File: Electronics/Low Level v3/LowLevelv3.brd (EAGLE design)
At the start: 117.3 x 68.1 mm, 58 parts, among them IC2 MCP4802, K1 ORWH-SH-105D1F,000, K3 ORWH-SH-105D1F,000, Q1 16MHz, T1 2N3904, T2 2N3904, U1 284512-4, U4 MCP2515, U5 MCP2551DIL08, X3 Motor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

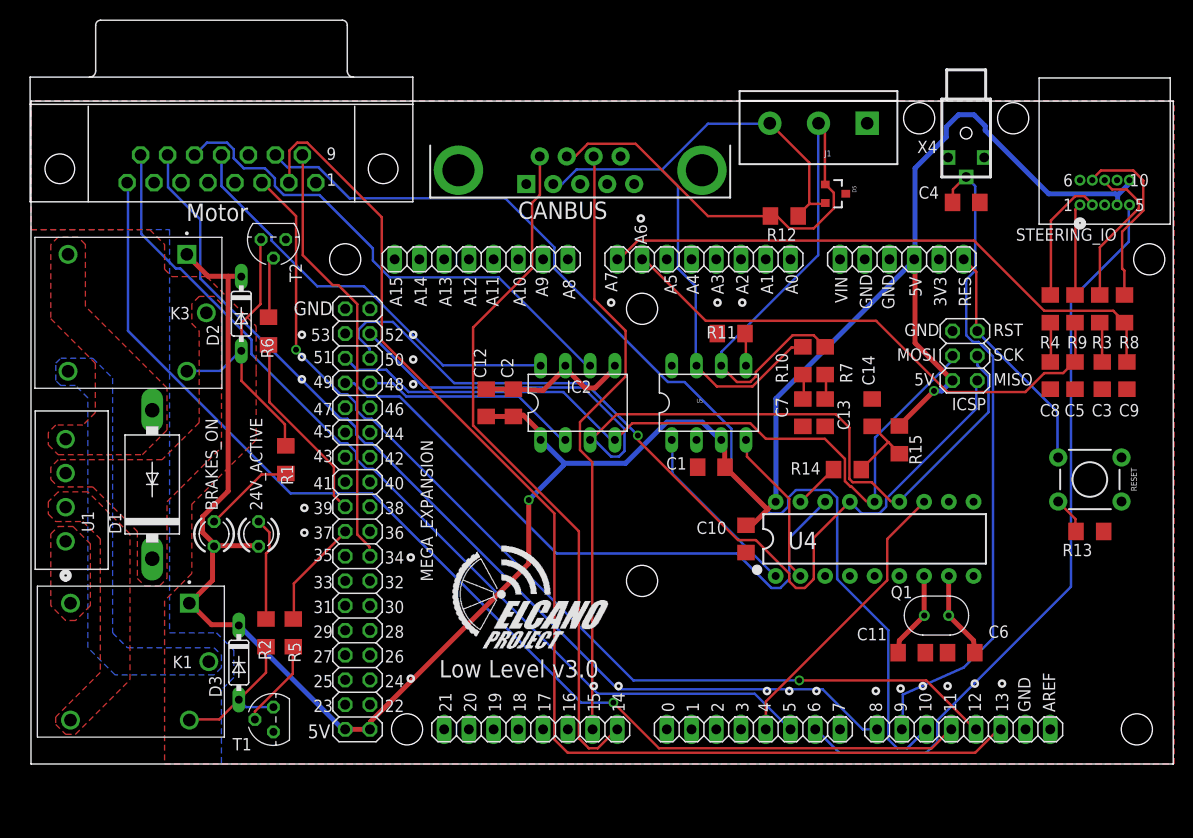
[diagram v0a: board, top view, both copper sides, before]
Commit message: Added e-stop, routed additional connetions to DB15, changed board layout
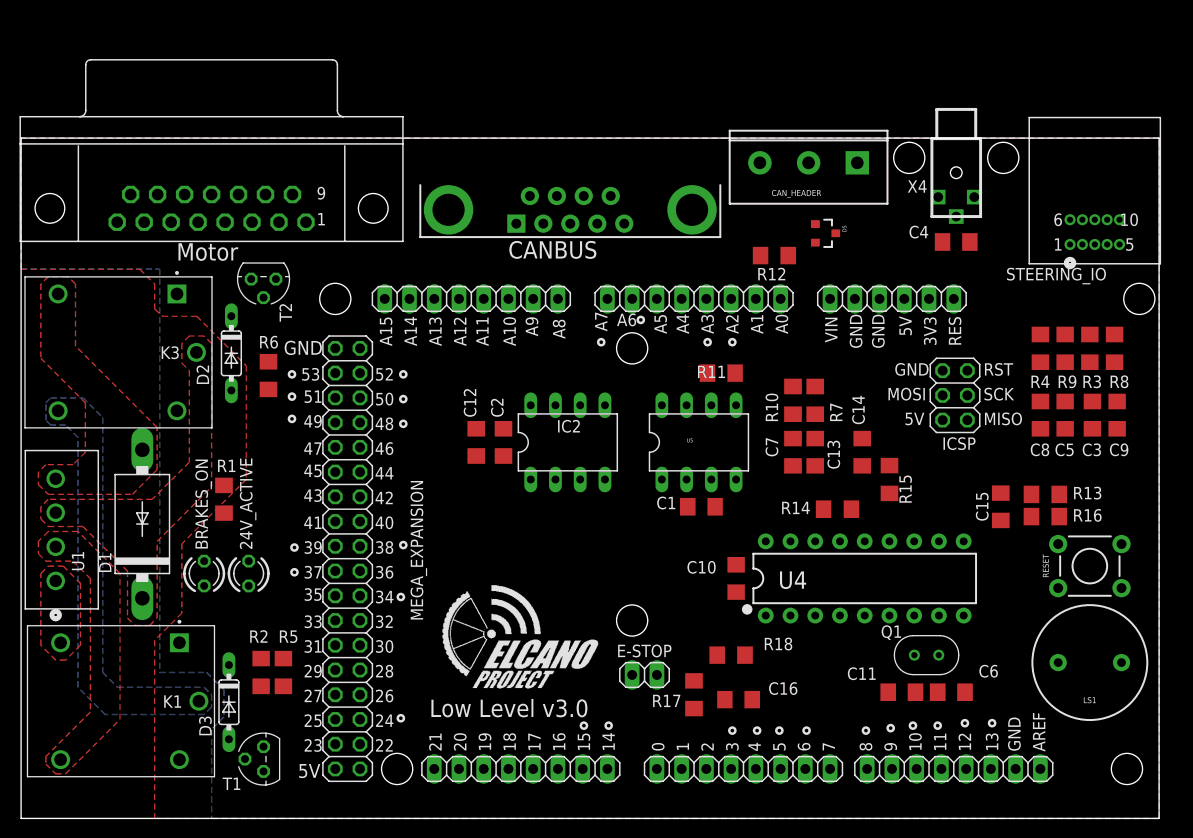
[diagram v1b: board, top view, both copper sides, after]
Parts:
- removed J1: (no value), SparkFun-Connectors:SCREWTERMINAL-5MM-3
- added C15, C16: 200nF, resistor:C1206
- added CAN_HEADER: (no value), SparkFun-Connectors:SCREWTERMINAL-5MM-3
- added E-STOP: (no value), pinhead:1X02
- added LS1: BUZZER-PTH, SparkFun-Electromechanical:BUZZER-12MM
- added R16, R17, R18: 10k, resistor:R1206
- R13: value 1K -> 10k
- moved RESET 8.89 mm to (109.7, 25.9), turned to 180 degrees
- moved R1 7.54 mm to (20.8, 32.8)
- moved R13 5.95 mm to (105.2, 33.3), turned to 0 degrees
- moved R6 4.57 mm to (25.4, 45.5)
- moved D5 4.19 mm to (82.5, 60.1)
- moved X4 4.19 mm to (96.0, 66.3)
- moved X3 4.19 mm to (19.6, 72.1)
- moved ADCL 4.19 mm to (69.1, 53.3)
- moved C1 4.19 mm to (69.8, 32.0)
- moved C12 4.19 mm to (46.7, 38.6)
- moved C14 4.19 mm to (86.4, 37.6)
- moved C3 4.19 mm to (110.0, 41.4)
- moved C4 4.19 mm to (96.0, 59.2)
- moved C8 4.19 mm to (104.6, 41.4)
- moved CANBUS 4.19 mm to (56.4, 62.5)
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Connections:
- net N$17 renamed OSC1
- net N$18 renamed OSC2
- removed net STR_L: ADCL.6
- removed net STR_R: ADCL.5
- new net BRAKE_PWM: DIGITAL_0-7.3, X3.1
- new net BUZZER: LS1.+, MEGA_EXPANSION.18
- new net D_36: MEGA_EXPANSION.20, X3.7
- new net ESTOP_INT: C16.1, DIGITAL_0-7.4, R17.1, X3.6
- new net N$8: E-STOP.2, R17.2, R18.1
- new net REGEN_ACTIVE: MEGA_EXPANSION.34, X3.5
- new net RX0: DIGITAL_0-7.1
- new net TX0: DIGITAL_0-7.2
- net 5V: now also E-STOP.1, RESET.1
- net CANH: now also CAN_HEADER.2; no longer J1.2
- net CANL: now also CAN_HEADER.3; no longer J1.3
- net GND: now also C15.2, C16.2, CAN_HEADER.1, LS1.-, R16.2, R18.2, U4.4, U4.5, U4.6; no longer J1.1, R13.1
- net L_SENSE: now also ADCL.6
- net N$1: now also R16.1
- net RESET: now also C15.1, R13.1; no longer RESET.1
- net REVERSE: now also X3.4
- net R_SENSE: now also ADCL.5
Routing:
- net 5V: track 241.2 -> 0.00 mm, vias 2 -> 0
- net HALLPHASEA: track 124.6 -> 0.00 mm
- net HALLPHASEC: track 118.4 -> 0.00 mm, vias 1 -> 0
- net EBIKECONTRL: track 110.9 -> 0.00 mm
- net HALLPHASEB: track 105.0 -> 0.00 mm, vias 2 -> 0
- net SPEEDOMETER: track 103.1 -> 0.00 mm
- net WATCHDOG: track 97.1 -> 0.00 mm
- net SCK: track 95.8 -> 0.00 mm
- net MISO: track 93.8 -> 0.00 mm, vias 1 -> 0
- net CANH: track 85.0 -> 0.00 mm
- net MOSI: track 81.5 -> 0.00 mm
- net STEER_SERVO_PWM: track 77.3 -> 0.00 mm
- net CANL: track 73.4 -> 0.00 mm
- net TX3: track 72.3 -> 0.00 mm
- net WHEELROTATION: track 67.6 -> 0.00 mm
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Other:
- board size 117.3 x 68.1 mm -> 116.8 x 69.8 mm

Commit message: partial routing, adding restrict polys
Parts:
- moved R11 3.34 mm to (75.2, 46.2), turned to 90 degrees
- moved R12 1.85 mm to (75.6, 58.3), turned to 90 degrees
- moved E-STOP 1.48 mm to (65.3, 15.5)
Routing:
- net 5V: track 0.00 -> 209.4 mm
- net HALLPHASEC: track 0.00 -> 138.1 mm, vias 0 -> 1
- net GND: track 0.00 -> 130.0 mm, vias 0 -> 4
- net WATCHDOG: track 0.00 -> 119.4 mm, vias 0 -> 1
- net SPEEDOMETER: track 0.00 -> 116.5 mm, vias 0 -> 1
- net HALLPHASEA: track 0.00 -> 114.9 mm, vias 0 -> 1
- net HALLPHASEB: track 0.00 -> 113.7 mm, vias 0 -> 1
- net EBIKECONTRL: track 0.00 -> 111.3 mm, vias 0 -> 1
- net REGEN_ACTIVE: track 0.00 -> 106.4 mm
- net SCK: track 0.00 -> 101.3 mm, vias 0 -> 2
- net ESTOP_INT: track 0.00 -> 101.1 mm, vias 0 -> 2
- net MISO: track 0.00 -> 91.0 mm, vias 0 -> 2
- net MOSI: track 0.00 -> 84.9 mm, vias 0 -> 2
- net BRAKE_PWM: track 0.00 -> 78.8 mm
- net CANH: track 0.00 -> 71.9 mm, vias 0 -> 1
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
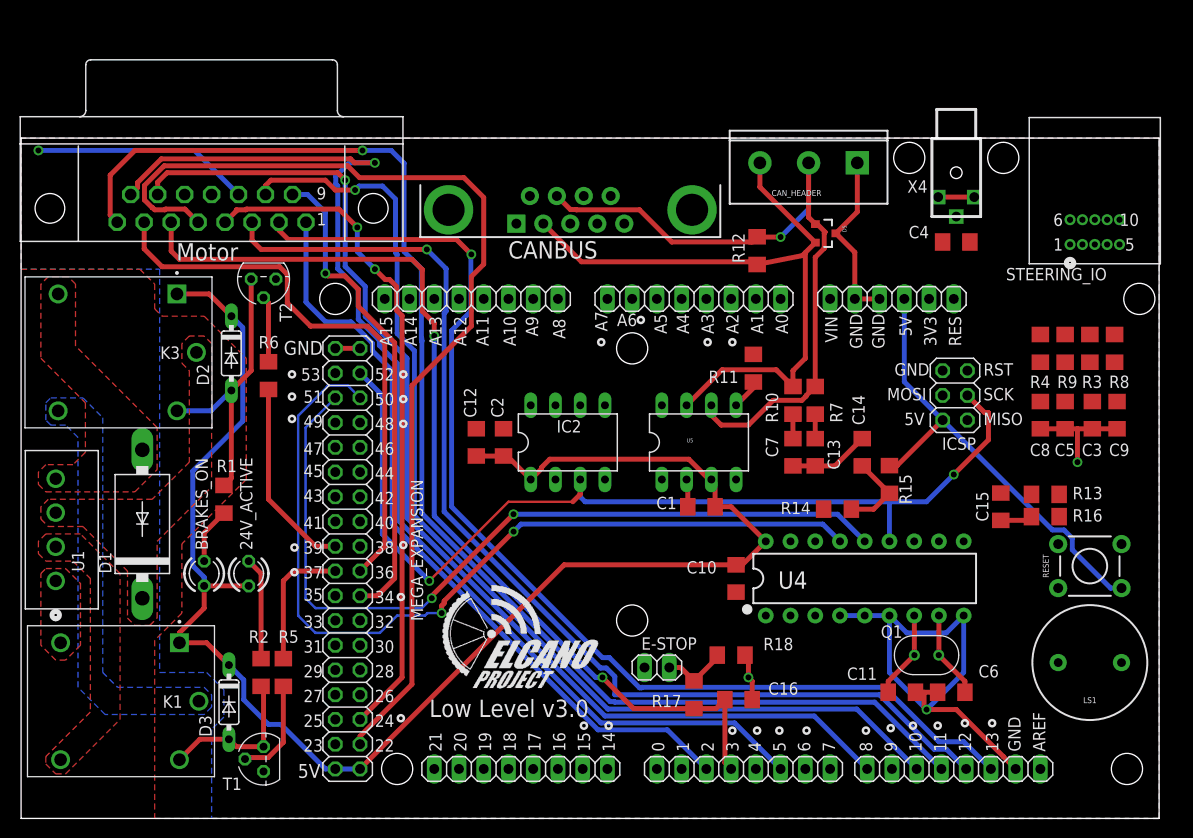
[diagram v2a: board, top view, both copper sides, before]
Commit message: LLBv3 routing overhaul
applied restriction polygons and added many vias to prevent GND airwires
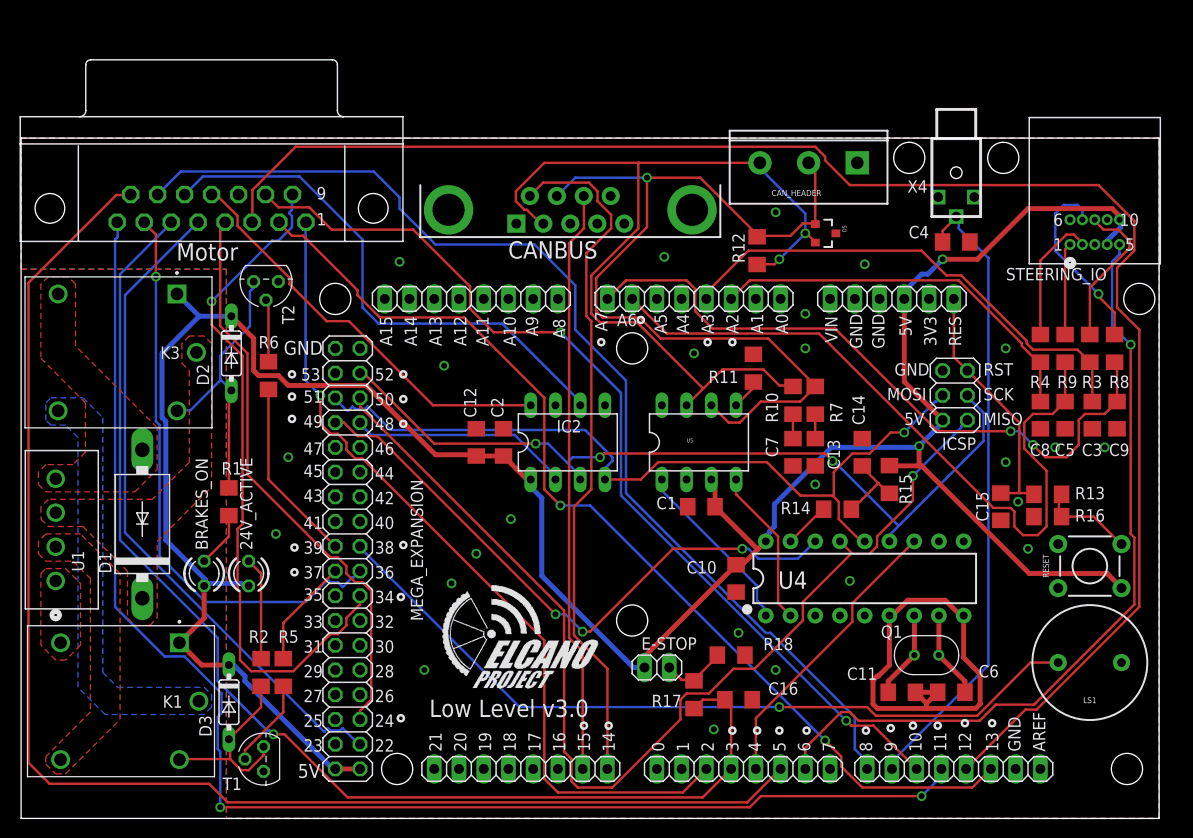
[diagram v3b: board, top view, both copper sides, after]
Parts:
- moved R1 0.57 mm to (21.3, 32.5)
- moved T2 0.36 mm to (25.1, 55.1)
- moved R13 0.25 mm to (105.4, 33.3)
- moved R16 0.25 mm to (105.4, 31.0)
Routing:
- net GND: track 130.0 -> 46.0 mm, vias 4 -> 25
- net BUZZER: track 0.00 -> 81.2 mm, vias 0 -> 1
- net STEER_SERVO_PWM: track 0.00 -> 81.0 mm, vias 0 -> 1
- net L_RTN_GND: track 0.00 -> 74.6 mm
- net TX3: track 0.00 -> 71.2 mm
- net R_RTN_GND: track 0.00 -> 70.0 mm, vias 0 -> 2
- net WHEELROTATION: track 0.00 -> 65.4 mm
- net CAN_SS: track 0.00 -> 62.8 mm, vias 0 -> 3
- net RX3: track 0.00 -> 60.0 mm
- net 5V: track 209.4 -> 266.3 mm, vias 0 -> 2
- net DACB: track 0.00 -> 55.4 mm
- net HALLPHASEB: track 113.7 -> 165.1 mm, vias 1 -> 0
- net R_SENSE: track 0.00 -> 50.8 mm
- net DACA: track 0.00 -> 42.7 mm
- net L_SENSE: track 0.00 -> 40.3 mm
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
